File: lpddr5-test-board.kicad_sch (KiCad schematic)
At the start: 13 parts, among them M1001 Mech_Lightpipe_Mentor_1296.20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

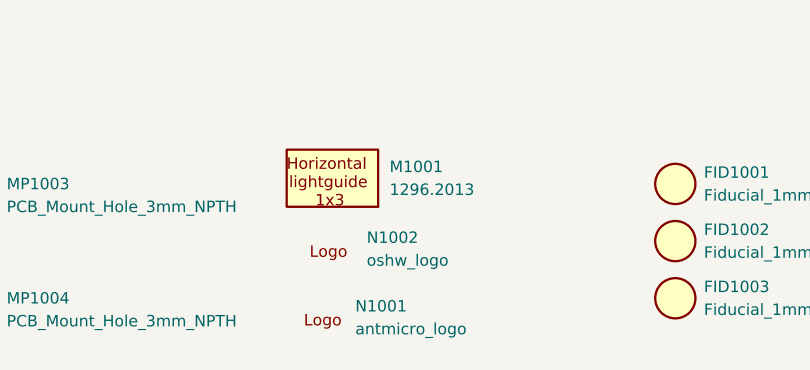
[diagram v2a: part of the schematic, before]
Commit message: Schematic cleanup, connect VINT DC-DC, continue placing misc. circuits
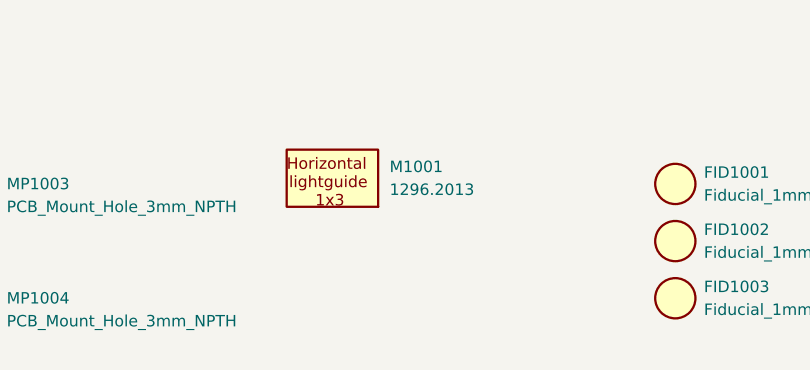
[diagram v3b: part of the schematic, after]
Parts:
- removed N1001: antmicro_logo, data-center-rdimm-ddr4-tester-footprints:antmicro-logo_scaled_20mm_mask, symbol data-center-rdimm-ddr4-tester:antmicro_logo
- removed N1002: oshw_logo, data-center-rdimm-ddr4-tester-footprints:oshw-logo, symbol data-center-rdimm-ddr4-tester:oshw_logo
